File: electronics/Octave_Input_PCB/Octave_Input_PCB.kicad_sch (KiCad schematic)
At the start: 67 parts, among them J1 HRO_TYPE-C-31-M-12, SW1 SW_Hot_Swap_Socket, SW10 SW_Hot_Swap_Socket, SW11 SW_Hot_Swap_Socket, SW12 SW_Hot_Swap_Socket, SW13 SW_Hot_Swap_Socket, SW14 Alps_Alpine_RKJXV1224, SW15 Bourns_PEC12R-4xxxF-Sxxx, SW2 SW_Hot_Swap_Socket, SW21 Alps_Alpine_SKRP, SW22 Alps_Alpine_SKRP, SW3 SW_Hot_Swap_Socket, SW4 SW_Hot_Swap_Socket, SW5 SW_Hot_Swap_Socket, SW6 SW_Hot_Swap_Socket, SW7 SW_Hot_Swap_Socket, SW8 SW_Hot_Swap_Socket, SW9 SW_Hot_Swap_Socket, U1 AP2112K-3.3, U2 Raspberry_Pi_RP2040, U3 W25Q64JVSS, Y1 12MHz

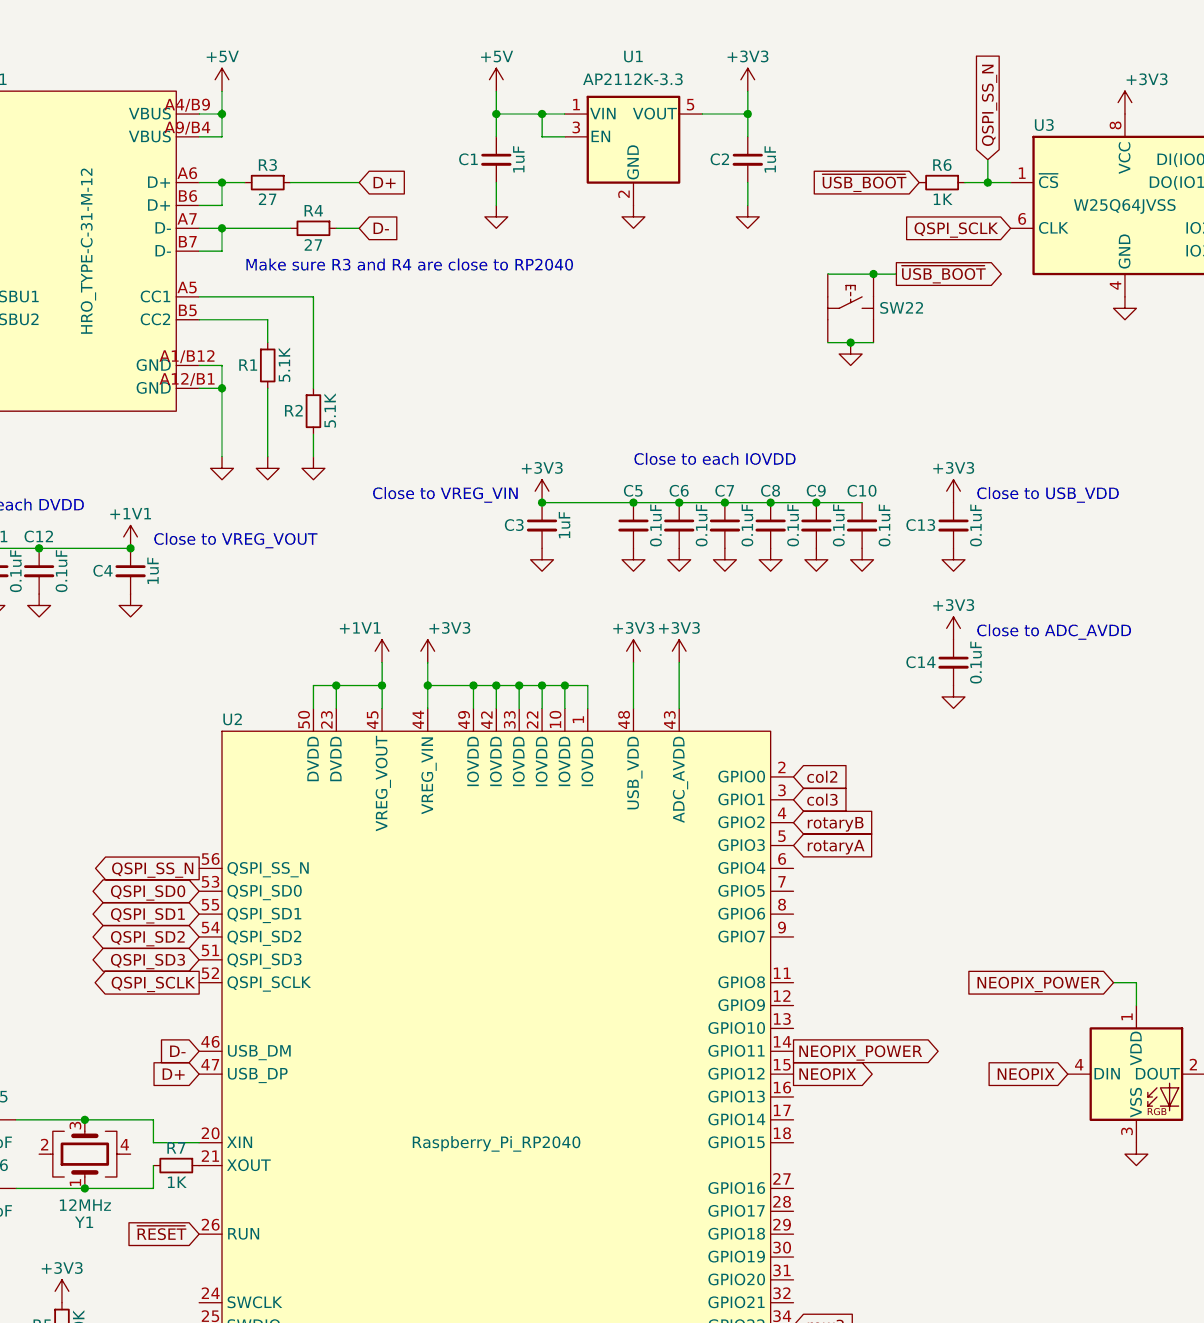
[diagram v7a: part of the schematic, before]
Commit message: Add pull-up for QSPI_SS_N
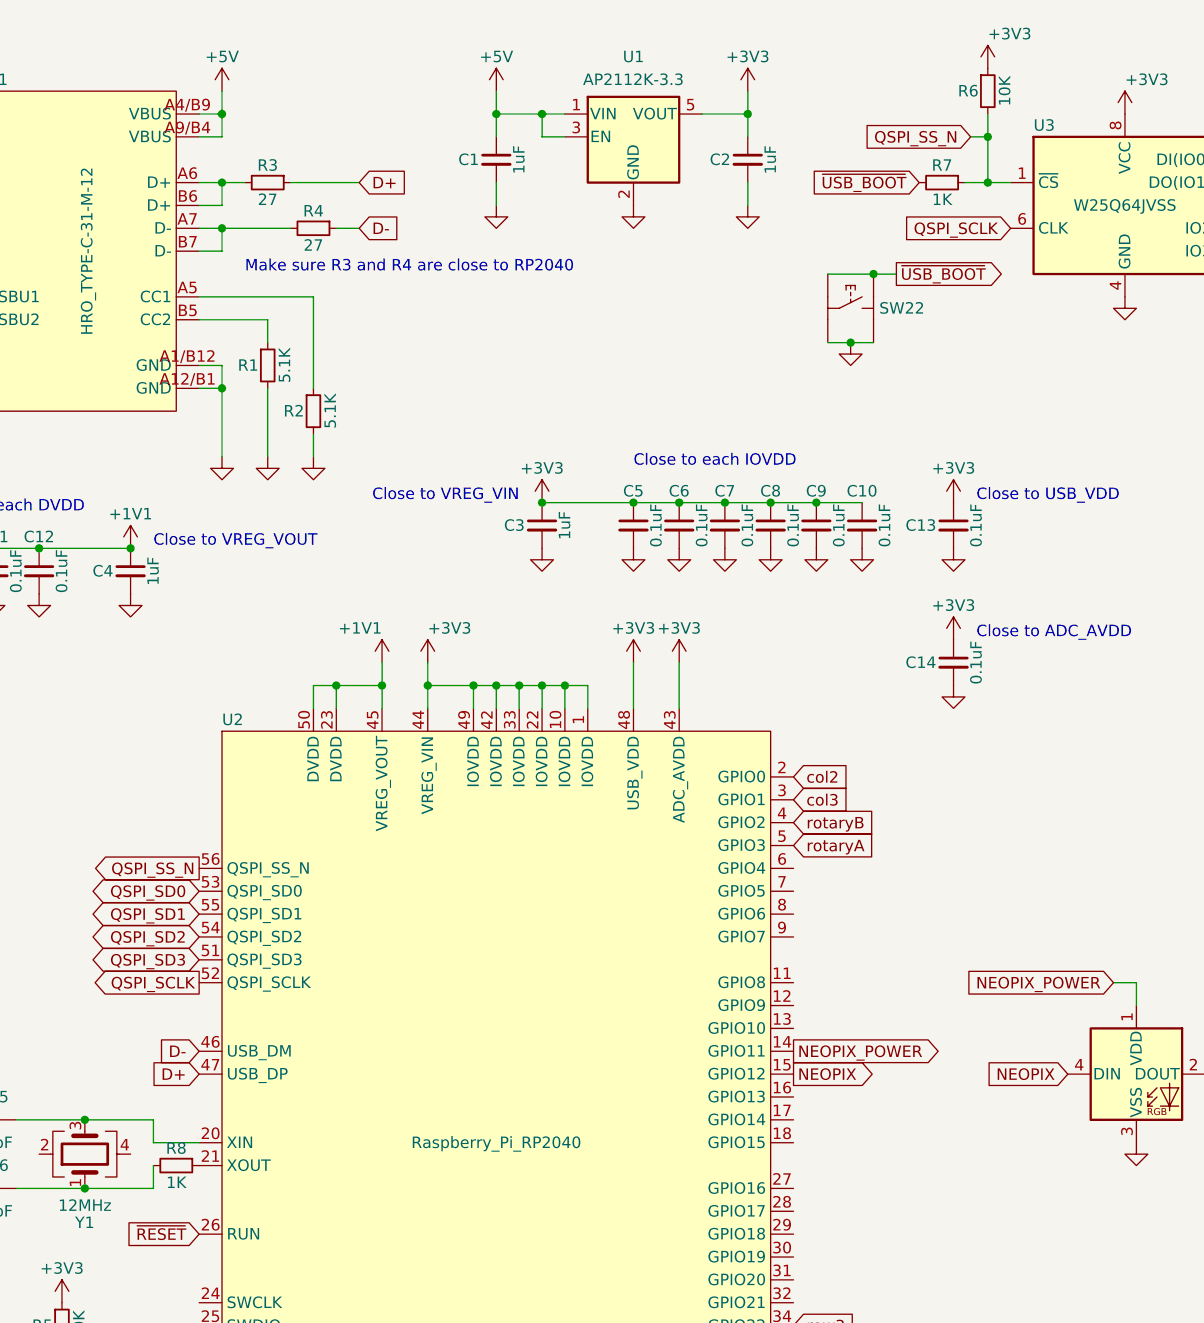
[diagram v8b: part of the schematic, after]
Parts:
- added R6: 10K, Resistor_SMD:R_0402_1005Metric, symbol Device:R_Small
- renumbered R6 to R7, R7 to R8
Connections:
- net +3V3: now also R6.1
- net QSPI_SS_N: now also R6.2
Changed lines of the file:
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@@
   (junction (at 78.74 91.44) (diameter 0) (color 0 0 0 0)
   )
+  (junction (at 135.89 30.48) (diameter 0) (color 0 0 0 0)
+  )
   (junction (at 251.46 149.86) (diameter 0) (color 0 0 0 0)
   )
@@
     (stroke (width 0) (type default) (color 0 0 0 0))
   )
+  (wire (pts (xy 133.985 30.48) (xy 135.89 30.48))
+    (stroke (width 0) (type default) (color 0 0 0 0))
+  )
   (wire (pts (xy 81.28 91.44) (xy 81.28 93.98))
     (stroke (width 0) (type default) (color 0 0 0 0))
@@
     (stroke (width 0) (type default) (color 0 0 0 0))
   )
+  (wire (pts (xy 135.89 30.48) (xy 135.89 35.56))
+    (stroke (width 0) (type default) (color 0 0 0 0))
+  )
   (wire (pts (xy 50.8 25.4) (xy 50.8 27.94))
     (stroke (width 0) (type default) (color 0 0 0 0))
@@
     (stroke (width 0) (type default) (color 0 0 0 0))
   )
-  (wire (pts (xy 135.89 33.02) (xy 135.89 35.56))
+  (wire (pts (xy 135.89 27.94) (xy 135.89 30.48))
     (stroke (width 0) (type default) (color 0 0 0 0))
   )
@@
     )
   )
-  (global_label "QSPI_SS_N" (shape input) (at 135.89 33.02 90) (fields_autoplaced)
-    (effects (font (size 1.27 1.27)) (justify left))
-    (property "Intersheet References" "${INTERSHEET_REFS}" (id 0) (at 135.9694 20.5074 90)
-      (effects (font (size 1.27 1.27)) (justify left) hide)
+  (global_label "QSPI_SS_N" (shape input) (at 133.985 30.48 180) (fields_autoplaced)
+    (effects (font (size 1.27 1.27)) (justify right))
+    (property "Intersheet References" "${INTERSHEET_REFS}" (id 0) (at 121.4724 30.4006 0)
+      (effects (font (size 1.27 1.27)) (justify right) hide)
     )
   )
@@
   (symbol (lib_id "Device:R_Small") (at 130.81 35.56 270) (unit 1)
     (in_bom yes) (on_board yes)
-    (property "Reference" "R6" (id 0) (at 130.81 33.655 90))
+    (property "Reference" "R7" (id 0) (at 130.81 33.655 90))
     (property "Value" "1K" (id 1) (at 130.81 37.465 90))
     (property "Footprint" "Resistor_SMD:R_0402_1005Metric" (id 2) (at 130.81 35.56 0)
@@
   (symbol (lib_id "Device:R_Small") (at 45.72 144.78 270) (unit 1)
     (in_bom yes) (on_board yes)
-    (property "Reference" "R7" (id 0) (at 45.72 142.875 90))
+    (property "Reference" "R8" (id 0) (at 45.72 142.875 90))
     (property "Value" "1K" (id 1) (at 45.72 146.685 90))
     (property "Footprint" "Resistor_SMD:R_0402_1005Metric" (id 2) (at 45.72 144.78 0)
@@
     )
     (property "Datasheet" "https://www.vishay.com/docs/85751/1n4148ws.pdf" (id 3) (at 210.82 36.83 0)
+      (effects (font (size 1.27 1.27)) hide)
+    )
+    (pin "1")
+    (pin "2")
+  )
+  (symbol (lib_id "Device:R_Small") (at 135.89 25.4 0) (unit 1)
+    (in_bom yes) (on_board yes)
+    (property "Reference" "R6" (id 0) (at 134.874 25.4 0)
+      (effects (font (size 1.27 1.27)) (justify right))
+    )
+    (property "Value" "10K" (id 1) (at 137.795 25.4 90))
+    (property "Footprint" "Resistor_SMD:R_0402_1005Metric" (id 2) (at 135.89 25.4 0)
+      (effects (font (size 1.27 1.27)) hide)
+    )
+    (property "Datasheet" "~" (id 3) (at 135.89 25.4 0)
       (effects (font (size 1.27 1.27)) hide)
     )
@@
     (pin "2")
   )
+  (symbol (lib_id "power:+3V3") (at 135.89 22.86 0) (unit 1)
+    (in_bom yes) (on_board yes)
+    (property "Reference" "#PWR0145" (id 0) (at 135.89 26.67 0)
+      (effects (font (size 1.27 1.27)) hide)
+    )
+    (property "Value" "+3V3" (id 1) (at 135.89 19.05 0)
+      (effects (font (size 1.27 1.27)) (justify left))
+    )
+    (property "Footprint" "" (id 2) (at 135.89 22.86 0)
+      (effects (font (size 1.27 1.27)) hide)
+    )
+    (property "Datasheet" "" (id 3) (at 135.89 22.86 0)
+      (effects (font (size 1.27 1.27)) hide)
+    )
+    (pin "1")
+  )
   (symbol (lib_id "power:GND") (at 236.22 106.68 0) (unit 1)
     (in_bom yes) (on_board yes) (fields_autoplaced)
@@
       (reference "#PWR0144") (unit 1) (value "GND") (footprint "")
     )
+    (path "/9056521e-b244-469a-ba8b-9e1553523fc6"
+      (reference "#PWR0145") (unit 1) (value "+3V3") (footprint "")
+    )
     (path "/b4a74826-80b4-490c-898e-4ec787ca4628"
       (reference "C1") (unit 1) (value "1uF") (footprint "Capacitor_SMD:C_0402_1005Metric")
@@
       (reference "R5") (unit 1) (value "10K") (footprint "Resistor_SMD:R_0402_1005Metric")
     )
+    (path "/3f59f9d0-66b2-4f21-a5ed-8e7a17415a71"
+      (reference "R6") (unit 1) (value "10K") (footprint "Resistor_SMD:R_0402_1005Metric")
+    )
     (path "/14b72ef2-bcd8-40a8-bd48-b14a04b1b91a"
-      (reference "R6") (unit 1) (value "1K") (footprint "Resistor_SMD:R_0402_1005Metric")
+      (reference "R7") (unit 1) (value "1K") (footprint "Resistor_SMD:R_0402_1005Metric")
     )
     (path "/1f112e80-cd52-4c68-bd36-41327ae91f4d"
-      (reference "R7") (unit 1) (value "1K") (footprint "Resistor_SMD:R_0402_1005Metric")
+      (reference "R8") (unit 1) (value "1K") (footprint "Resistor_SMD:R_0402_1005Metric")
     )
     (path "/7f4d601a-fb1a-4382-a226-74a11a0738f3"
